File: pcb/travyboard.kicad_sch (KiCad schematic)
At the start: 0 parts

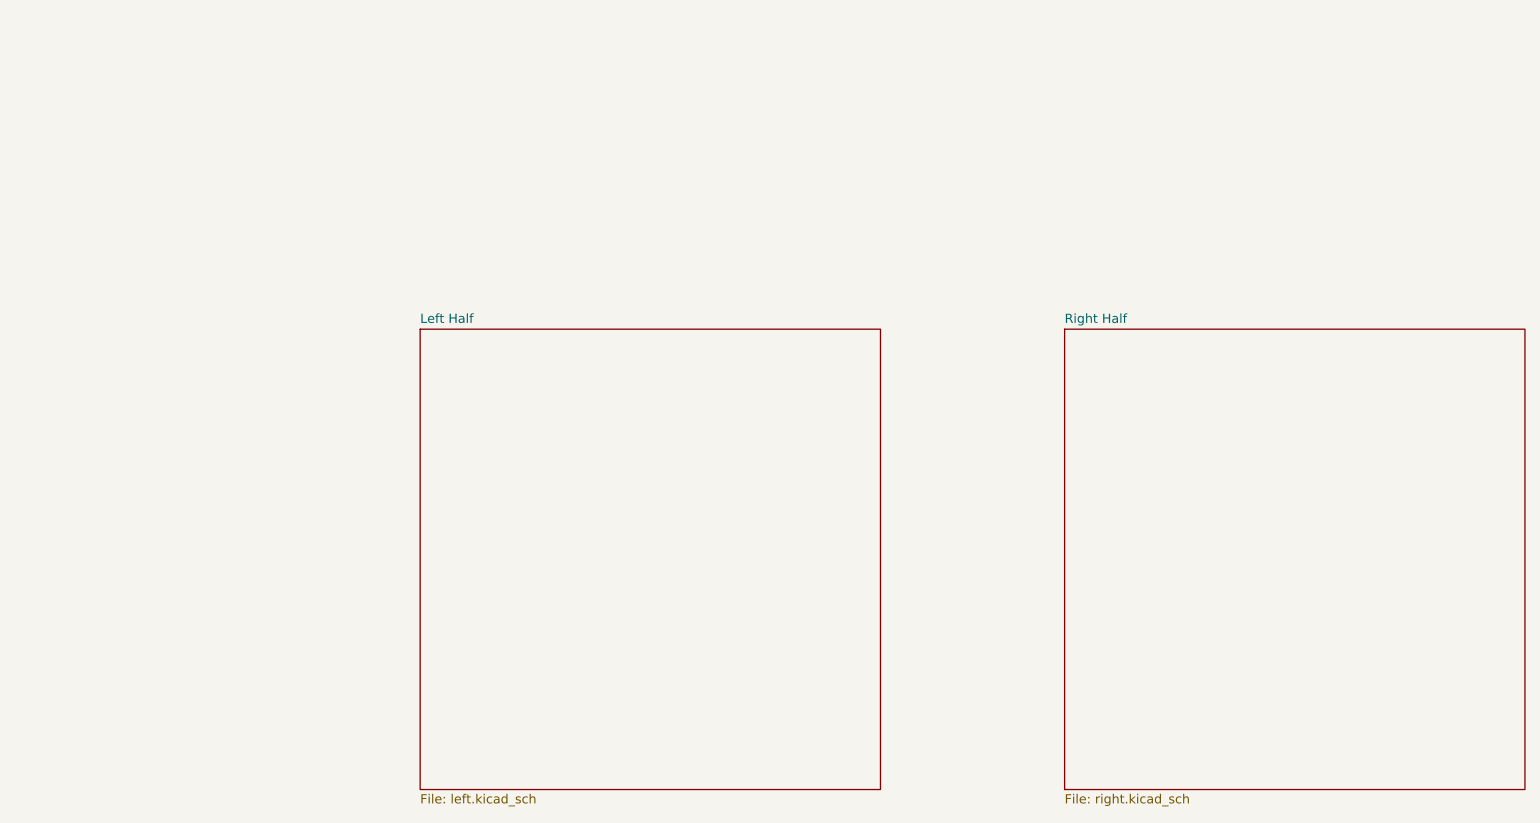
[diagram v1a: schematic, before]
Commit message: Remove kicad backups from git
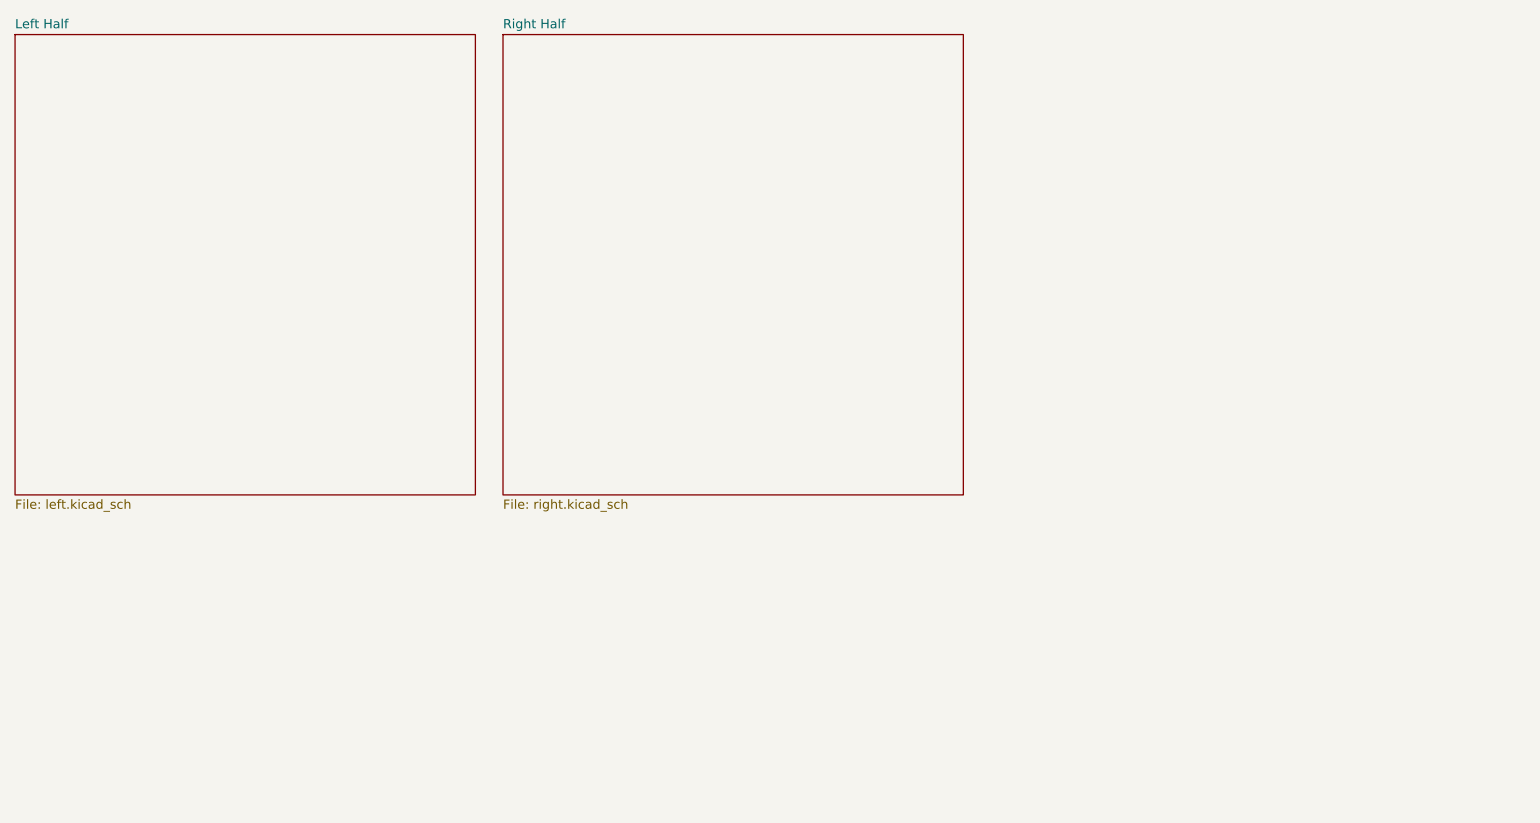
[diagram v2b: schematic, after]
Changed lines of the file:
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@@
 	(paper "A4")
 	(sheet
-		(at 76.2 63.5)
+		(at 20.32 22.86)
 		(size 63.5 63.5)
 		(exclude_from_sim no)
@@
 		)
 		(property "Sheetname" "Left Half"
-			(at 76.2 62.7884 0)
+			(at 20.32 22.1484 0)
 			(effects
 				(font
@@
 		)
 		(property "Sheetfile" "left.kicad_sch"
-			(at 76.2 127.5846 0)
+			(at 20.32 86.9446 0)
 			(effects
 				(font
@@
 	)
 	(sheet
-		(at 165.1 63.5)
+		(at 87.63 22.86)
 		(size 63.5 63.5)
 		(exclude_from_sim no)
@@
 		)
 		(property "Sheetname" "Right Half"
-			(at 165.1 62.7884 0)
+			(at 87.63 22.1484 0)
 			(effects
 				(font
@@
 		)
 		(property "Sheetfile" "right.kicad_sch"
-			(at 165.1 127.5846 0)
+			(at 87.63 86.9446 0)
 			(effects
 				(font
